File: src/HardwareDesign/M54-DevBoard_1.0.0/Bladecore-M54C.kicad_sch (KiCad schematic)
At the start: 17 parts, among them J1 MDT580M01001, J12 DE9_Socket_MountingHoles, J2 PINHD_1x10_Female, J3 PINHD_1x10_Female, J4 PINHD_1x10_Female, J5 PINHD_1x10_Female, J6 PINHD_1x10_Female, J7 PINHD_1x10_Female

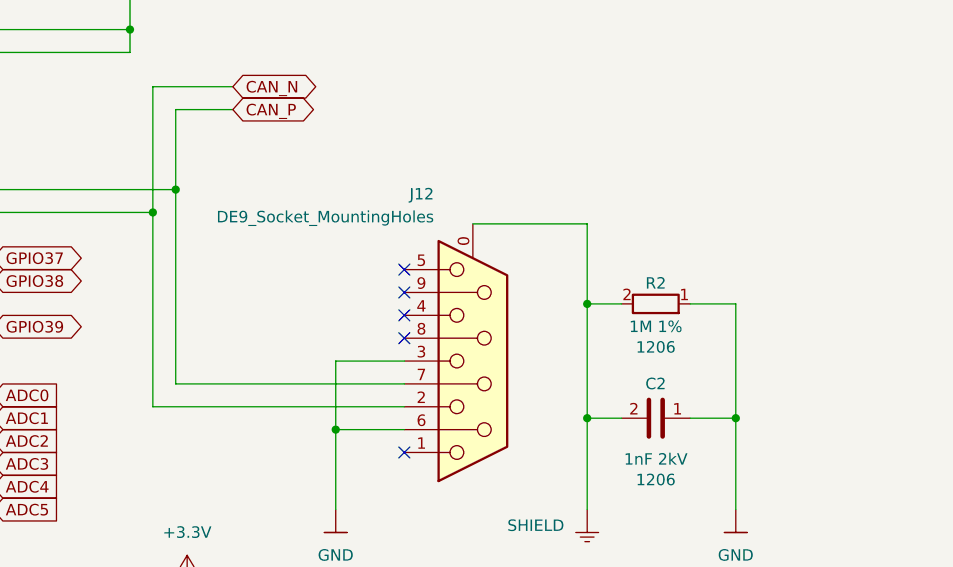
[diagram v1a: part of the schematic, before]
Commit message: fix hardware bugs, add software example
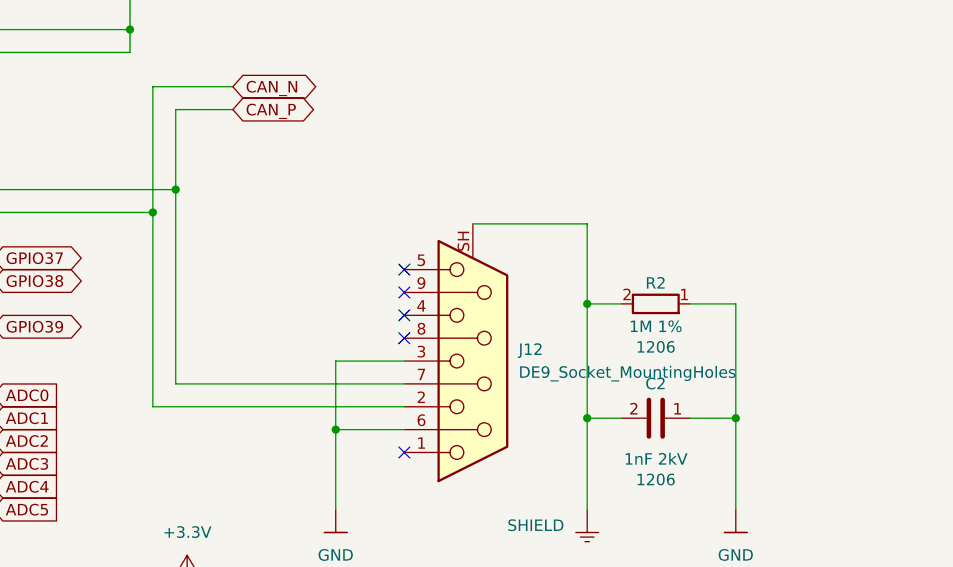
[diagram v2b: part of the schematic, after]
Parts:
- J12: footprint Connector_Dsub:DSUB-9_Socket_Horizontal_P2.77x2.84mm_EdgePinOffset4.94mm_Housed_MountingHolesOffset4.94mm -> Connector_Dsub:DSUB-9_Socket_Horizontal_P2.77x2.84mm_EdgePinOffset7.70mm_Housed_MountingHolesOffset9.12mm
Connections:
- net SHIELD: now also J12.SH (PAD); no longer J12.0 (PAD)

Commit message: scope measurements
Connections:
- net GND: now also J1.SH1 (SHIELD), J1.SH2 (SHIELD); no longer J1.S1 (SHIELD), J1.S2 (SHIELD)
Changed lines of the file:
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@@
 		(dnp no)
 		(fields_autoplaced yes)
-		(property "Reference" "#PWR07"
+		(property "Reference" "#PWR7"
 			(at 354.33 81.28 0)
 			(hide yes)
@@
 			(project "M54-DevBoard_1.0.0"
 				(path "/f9e05184-c88b-4a88-ae9c-ab2bdb32be7c/c5103ceb-5325-4a84-a025-9638a412984e/f06537ee-772d-44d3-8c50-e0ba41038c9c"
-					(reference "#PWR07")
+					(reference "#PWR7")
 					(unit 1)
 				)
@@
 			)
 		)
-		(property "Datasheet" ""
+		(property "Datasheet" "https://www.yageogroup.com/component-documentation/download/specsheet/C1206X102KGRACTU?lang=en"
 			(at 223.012 147.32 0)
 			(hide yes)
@@
 		(dnp no)
 		(fields_autoplaced yes)
-		(property "Reference" "#PWR03"
+		(property "Reference" "#PWR3"
 			(at 57.15 171.45 0)
 			(hide yes)
@@
 			(project "M54-DevBoard_1.0.0"
 				(path "/f9e05184-c88b-4a88-ae9c-ab2bdb32be7c/c5103ceb-5325-4a84-a025-9638a412984e/f06537ee-772d-44d3-8c50-e0ba41038c9c"
-					(reference "#PWR03")
+					(reference "#PWR3")
 					(unit 1)
 				)
@@
 		(dnp no)
 		(fields_autoplaced yes)
-		(property "Reference" "#PWR010"
+		(property "Reference" "#PWR10"
 			(at 295.91 81.28 0)
 			(hide yes)
@@
 			(project "M54-DevBoard_1.0.0"
 				(path "/f9e05184-c88b-4a88-ae9c-ab2bdb32be7c/c5103ceb-5325-4a84-a025-9638a412984e/f06537ee-772d-44d3-8c50-e0ba41038c9c"
-					(reference "#PWR010")
+					(reference "#PWR10")
 					(unit 1)
 				)
@@
 		(dnp no)
 		(fields_autoplaced yes)
-		(property "Reference" "#PWR012"
+		(property "Reference" "#PWR12"
 			(at 382.27 158.75 0)
 			(hide yes)
@@
 			(project "M54-DevBoard_1.0.0"
 				(path "/f9e05184-c88b-4a88-ae9c-ab2bdb32be7c/c5103ceb-5325-4a84-a025-9638a412984e/f06537ee-772d-44d3-8c50-e0ba41038c9c"
-					(reference "#PWR012")
+					(reference "#PWR12")
 					(unit 1)
 				)
@@
 		(dnp no)
 		(fields_autoplaced yes)
-		(property "Reference" "#PWR05"
+		(property "Reference" "#PWR5"
 			(at 172.72 82.55 0)
 			(hide yes)
@@
 			(project "M54-DevBoard_1.0.0"
 				(path "/f9e05184-c88b-4a88-ae9c-ab2bdb32be7c/c5103ceb-5325-4a84-a025-9638a412984e/f06537ee-772d-44d3-8c50-e0ba41038c9c"
-					(reference "#PWR05")
+					(reference "#PWR5")
 					(unit 1)
 				)
@@
 		(dnp no)
 		(fields_autoplaced yes)
-		(property "Reference" "#PWR011"
+		(property "Reference" "#PWR11"
 			(at 372.11 158.75 0)
 			(hide yes)
@@
 			(project "M54-DevBoard_1.0.0"
 				(path "/f9e05184-c88b-4a88-ae9c-ab2bdb32be7c/c5103ceb-5325-4a84-a025-9638a412984e/f06537ee-772d-44d3-8c50-e0ba41038c9c"
-					(reference "#PWR011")
+					(reference "#PWR11")
 					(unit 1)
 				)
@@
 		(dnp no)
 		(fields_autoplaced yes)
-		(property "Reference" "#PWR090"
+		(property "Reference" "#PWR90"
 			(at 179.07 165.1 0)
 			(hide yes)
@@
 			(project "M54-DevBoard_1.0.0"
 				(path "/f9e05184-c88b-4a88-ae9c-ab2bdb32be7c/c5103ceb-5325-4a84-a025-9638a412984e/f06537ee-772d-44d3-8c50-e0ba41038c9c"
-					(reference "#PWR090")
+					(reference "#PWR90")
 					(unit 1)
 				)
@@
 		(dnp no)
 		(fields_autoplaced yes)
-		(property "Reference" "#PWR091"
+		(property "Reference" "#PWR91"
 			(at 142.24 83.82 0)
 			(hide yes)
@@
 			(project "M54-DevBoard_1.0.0"
 				(path "/f9e05184-c88b-4a88-ae9c-ab2bdb32be7c/c5103ceb-5325-4a84-a025-9638a412984e/f06537ee-772d-44d3-8c50-e0ba41038c9c"
-					(reference "#PWR091")
+					(reference "#PWR91")
 					(unit 1)
 				)
@@
 		(pin "75"
 		)
-		(pin "S1"
-		)
-		(pin "S2"
+		(pin "SH1"
+		)
+		(pin "SH2"
 		)
 		(pin "1"
@@
 		(dnp no)
 		(fields_autoplaced yes)
-		(property "Reference" "#PWR02"
+		(property "Reference" "#PWR2"
 			(at 146.05 166.37 0)
 			(hide yes)
@@
 			(project "M54-DevBoard_1.0.0"
 				(path "/f9e05184-c88b-4a88-ae9c-ab2bdb32be7c/c5103ceb-5325-4a84-a025-9638a412984e/f06537ee-772d-44d3-8c50-e0ba41038c9c"
-					(reference "#PWR02")
+					(reference "#PWR2")
 					(unit 1)
 				)
@@
 		(dnp no)
 		(fields_autoplaced yes)
-		(property "Reference" "#PWR08"
+		(property "Reference" "#PWR8"
 			(at 363.22 158.75 0)
 			(hide yes)
@@
 			(project "M54-DevBoard_1.0.0"
 				(path "/f9e05184-c88b-4a88-ae9c-ab2bdb32be7c/c5103ceb-5325-4a84-a025-9638a412984e/f06537ee-772d-44d3-8c50-e0ba41038c9c"
-					(reference "#PWR08")
-					(unit 1)
-				)
+					(reference "#PWR8")
+					(unit 1)
+				)
